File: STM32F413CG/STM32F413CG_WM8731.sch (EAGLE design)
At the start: 59 parts, among them IC1 STM32F413CGU6, IC2 WM8731SEDS_RV, J2 1503_02, X1 USB-MICROB-SMD

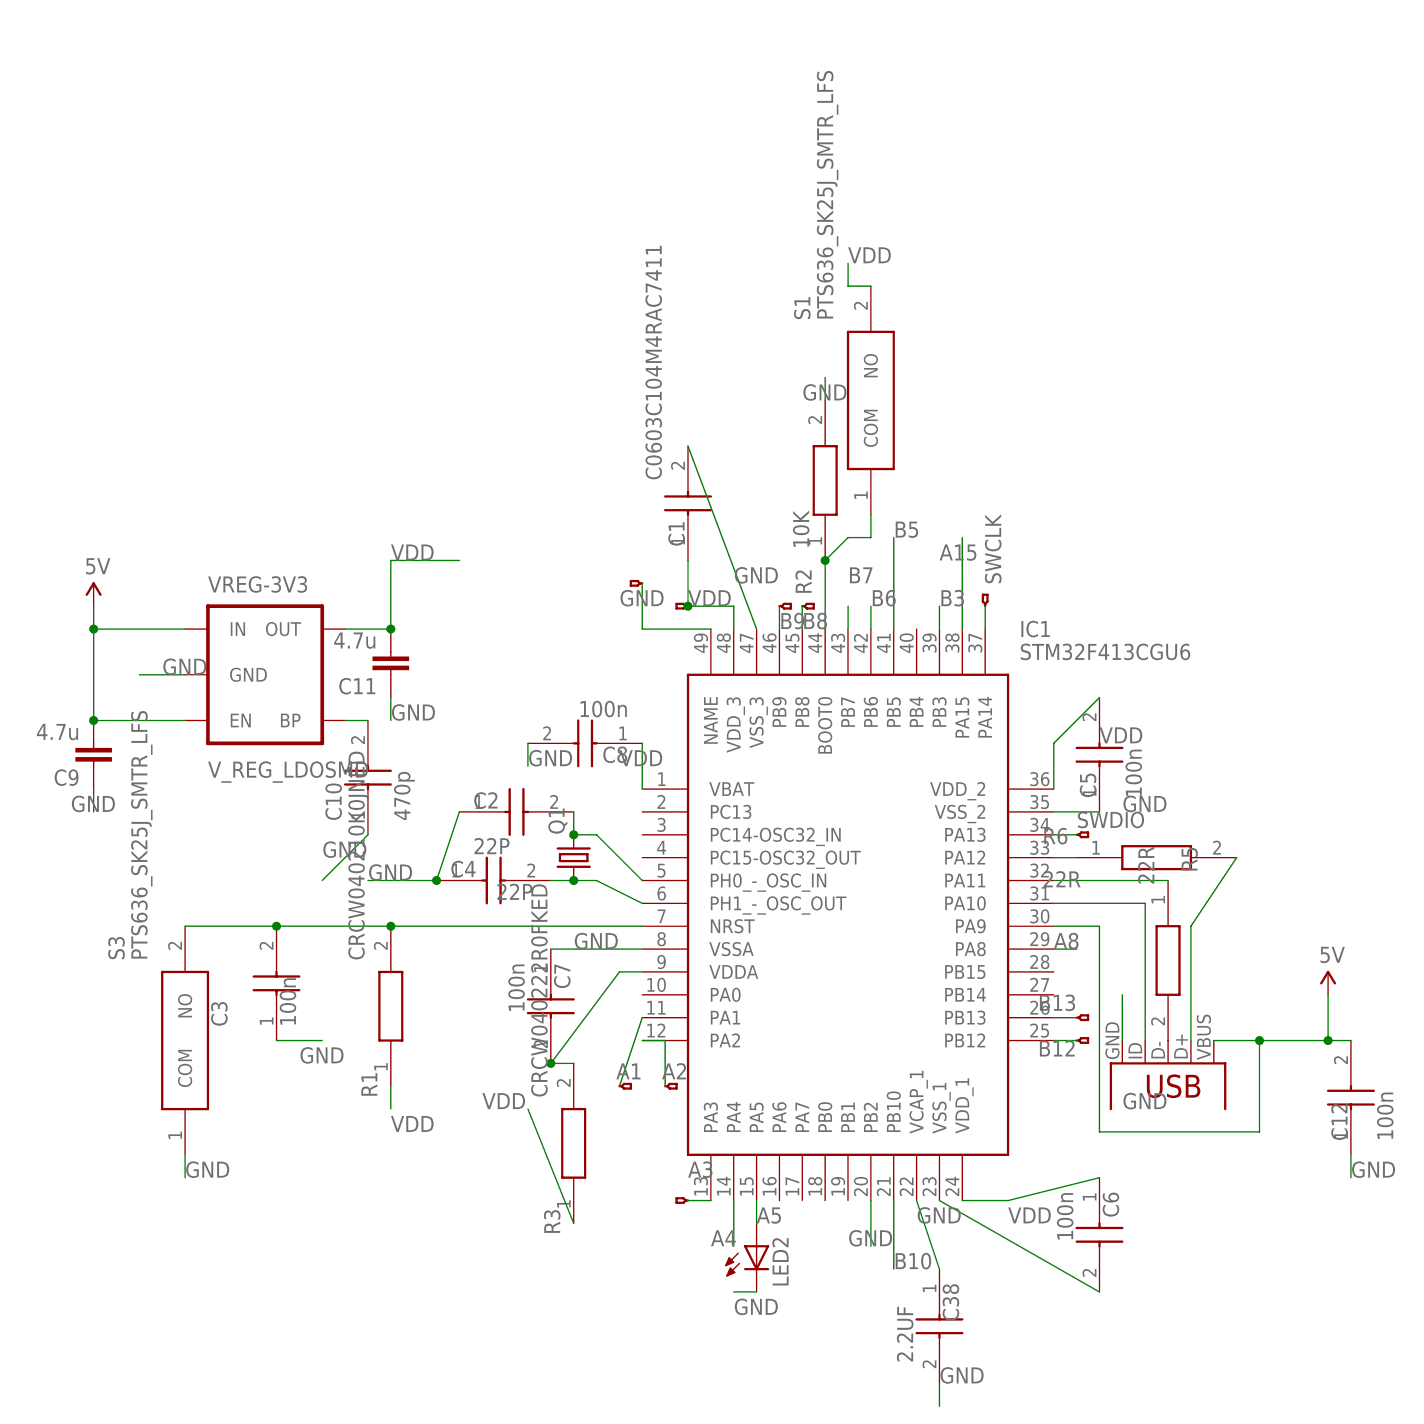
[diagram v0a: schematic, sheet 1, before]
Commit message: added STM32L451RE
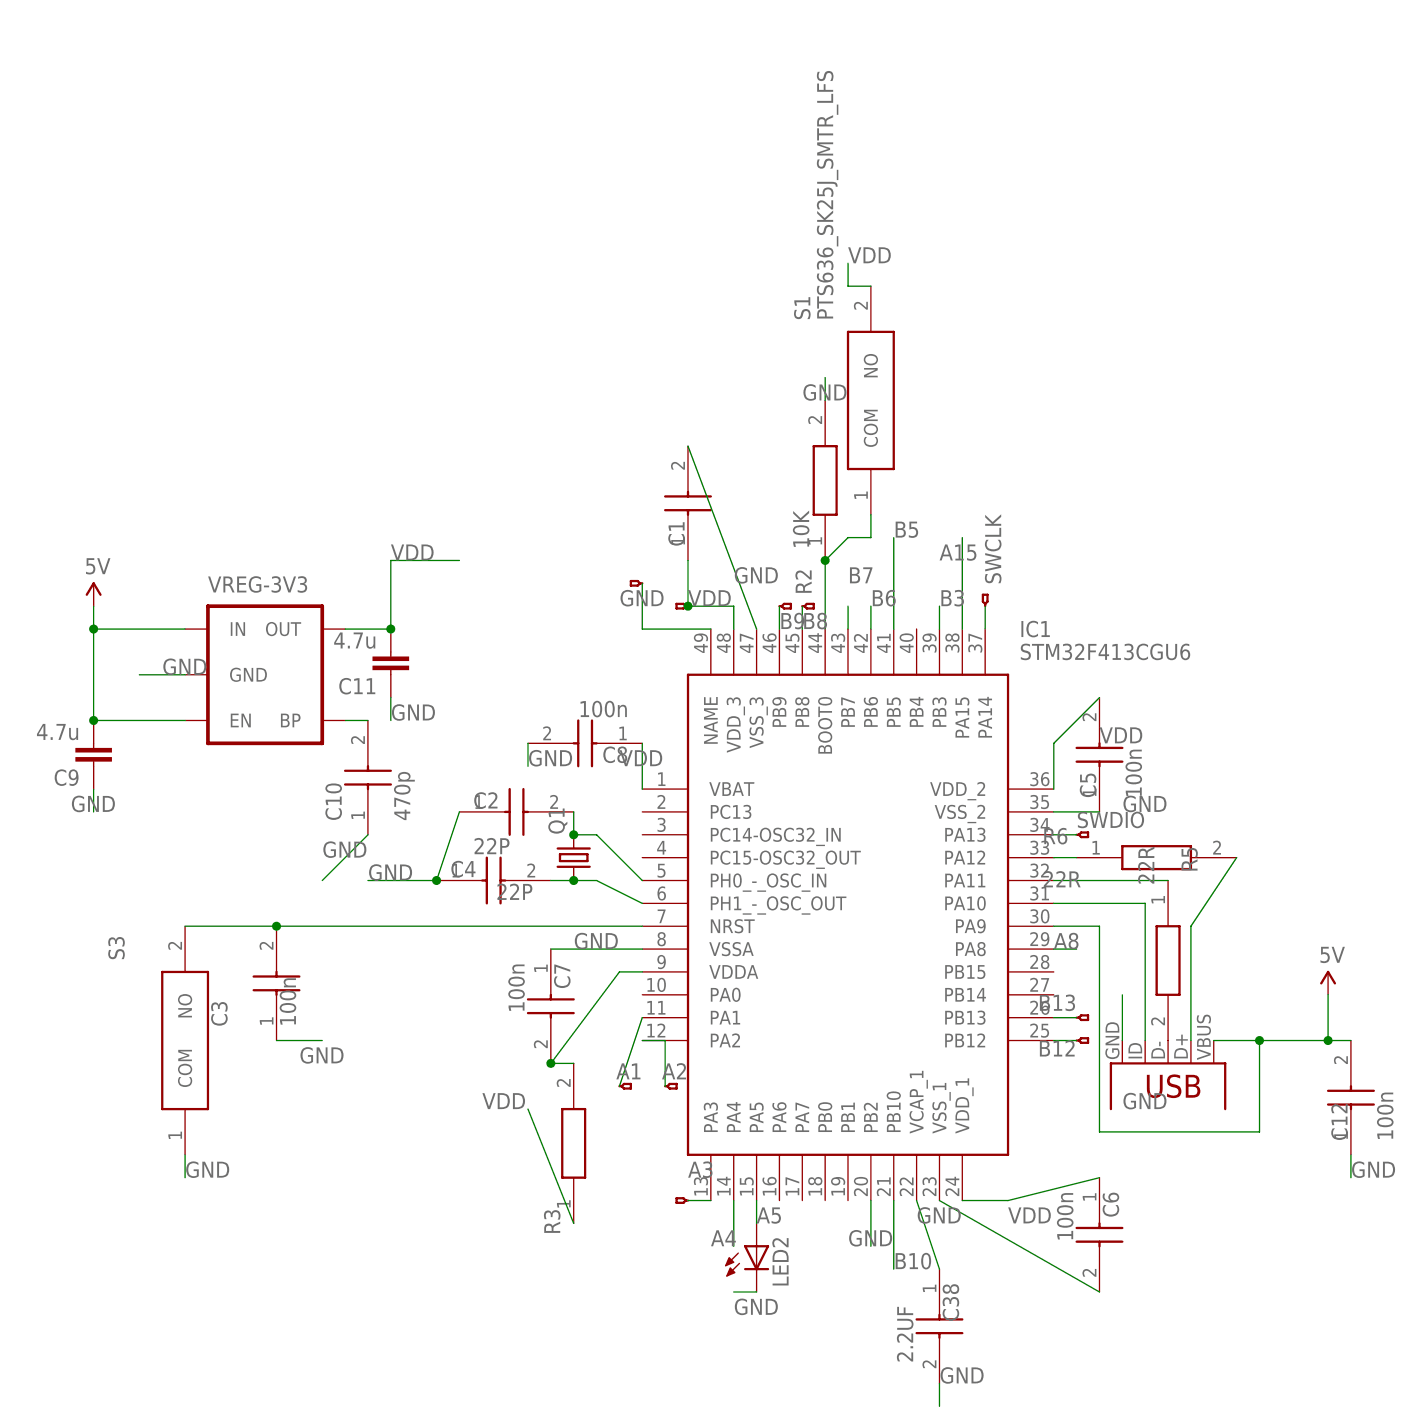
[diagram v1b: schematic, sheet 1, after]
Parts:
- removed R1: CRCW040210K0JNED, CRCW040210K0JNED:CRCW040210K0JNED
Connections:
- net N$3: no longer R1.2
- net VDD: no longer R1.1
